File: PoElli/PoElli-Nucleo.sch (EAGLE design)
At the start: 120 parts, among them CN10 NUCLEO-CN10, CN7 NUCLEO-CN7, J3 M022.54MM, J4 M022.54MM, Q3 FDMC2674, Q4 IRFL4310, SW1 A6H2101, SW2 A6H2101, T1 Coilcraft 230NL, T2 FLYBACK750311689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

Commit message: review changes applied
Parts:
- added R10: 100, ELL-i-Passives:R0603
- C21: value 100nF -> 100nF 100V
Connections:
- new net N$9: C21.2, R10.2
- net N$33: now also R10.1; no longer C21.2
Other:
- moved on the sheet: C21, D3, R16
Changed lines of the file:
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@@
 <part name="D3" library="ELL-i-DIscreteSemi" deviceset="BAV20WS" device=""/>
 <part name="R16" library="ELL-i-Passives" deviceset="R" device="1206" value="2k"/>
-<part name="C21" library="ELL-i-Passives" deviceset="C" device="0805" value="100nF"/>
+<part name="C21" library="ELL-i-Passives" deviceset="C" device="0805" value="100nF 100V"/>
 <part name="D17" library="ELL-i-DIscreteSemi" deviceset="DIODE-SCHOTTKY" device="B2100" value="B2100"/>
 <part name="D16" library="ELL-i-DIscreteSemi" deviceset="DIODE-SCHOTTKY" device="B2100" value="B2100"/>
@@
 <part name="D1" library="SparkFun-LED" deviceset="LED-GREEN" device="0603" value="GREEN"/>
 <part name="D2" library="SparkFun-LED" deviceset="LED-YELLOW" device="0603" value="YELLOW"/>
+<part name="R10" library="ELL-i-Passives" deviceset="R" device="0603" value="100"/>
 </parts>
 <sheets>
@@
 <text x="-17.78" y="83.82" size="1.778" layer="97" rot="R180">100V</text>
 <text x="10.16" y="60.96" size="1.778" layer="97">25V</text>
-<text x="2.54" y="104.14" size="1.778" layer="97" rot="R90">100V</text>
 <text x="-68.58" y="96.52" size="1.778" layer="97">R38 solder bridge is a potential
 alternative to R25, D11 and D13.
@@
 <instance part="C30" gate="G$1" x="10.16" y="66.04" rot="R90"/>
 <instance part="R34" gate="G$1" x="-5.08" y="12.7" rot="R90"/>
-<instance part="D3" gate="G$1" x="22.86" y="93.98" rot="R180"/>
-<instance part="R16" gate="G$1" x="-2.54" y="93.98" rot="R180"/>
-<instance part="C21" gate="G$1" x="-5.08" y="101.6" rot="R90"/>
+<instance part="D3" gate="G$1" x="20.32" y="93.98" rot="R180"/>
+<instance part="R16" gate="G$1" x="-5.08" y="93.98" rot="R180"/>
+<instance part="C21" gate="G$1" x="-10.16" y="101.6" rot="R90"/>
 <instance part="D17" gate="G$1" x="-160.02" y="22.86" rot="R90"/>
 <instance part="D16" gate="G$1" x="-165.1" y="22.86" rot="R90"/>
@@
 <instance part="D1" gate="G$1" x="185.42" y="180.34"/>
 <instance part="D2" gate="G$1" x="195.58" y="180.34"/>
+<instance part="R10" gate="G$1" x="2.54" y="101.6" rot="R180"/>
 </instances>
 <busses>
@@
 <junction x="27.94" y="53.34"/>
 <pinref part="D3" gate="G$1" pin="A"/>
-<wire x1="25.4" y1="93.98" x2="27.94" y2="93.98" width="0.1524" layer="91"/>
+<wire x1="22.86" y1="93.98" x2="27.94" y2="93.98" width="0.1524" layer="91"/>
 <junction x="27.94" y="93.98"/>
 <pinref part="T2" gate="G$1" pin="PRI+"/>
@@
 <net name="N$33" class="0">
 <segment>
-<pinref part="C21" gate="G$1" pin="2"/>
-<wire x1="12.7" y1="101.6" x2="0" y2="101.6" width="0.1524" layer="91"/>
 <pinref part="D3" gate="G$1" pin="C"/>
-<wire x1="20.32" y1="93.98" x2="12.7" y2="93.98" width="0.1524" layer="91"/>
-<wire x1="12.7" y1="101.6" x2="12.7" y2="93.98" width="0.1524" layer="91"/>
+<wire x1="17.78" y1="93.98" x2="10.16" y2="93.98" width="0.1524" layer="91"/>
+<wire x1="10.16" y1="101.6" x2="10.16" y2="93.98" width="0.1524" layer="91"/>
 <pinref part="R16" gate="G$1" pin="1"/>
-<wire x1="2.54" y1="93.98" x2="12.7" y2="93.98" width="0.1524" layer="91"/>
-<junction x="12.7" y="93.98"/>
+<wire x1="0" y1="93.98" x2="10.16" y2="93.98" width="0.1524" layer="91"/>
+<junction x="10.16" y="93.98"/>
+<pinref part="R10" gate="G$1" pin="1"/>
+<wire x1="7.62" y1="101.6" x2="10.16" y2="101.6" width="0.1524" layer="91"/>
 </segment>
 </net>
@@
 <wire x1="-40.64" y1="86.36" x2="-15.24" y2="86.36" width="0.1524" layer="91"/>
 <pinref part="U4" gate="G$1" pin="VIN"/>
-<wire x1="-15.24" y1="86.36" x2="-10.16" y2="86.36" width="0.1524" layer="91"/>
 <junction x="-15.24" y="86.36"/>
 <pinref part="C29" gate="G$1" pin="1"/>
 <pinref part="R16" gate="G$1" pin="2"/>
-<wire x1="-10.16" y1="86.36" x2="35.56" y2="86.36" width="0.1524" layer="91"/>
-<wire x1="-7.62" y1="93.98" x2="-10.16" y2="93.98" width="0.1524" layer="91"/>
+<wire x1="-15.24" y1="86.36" x2="35.56" y2="86.36" width="0.1524" layer="91"/>
+<wire x1="-10.16" y1="93.98" x2="-15.24" y2="93.98" width="0.1524" layer="91"/>
 <junction x="-15.24" y="86.36"/>
-<wire x1="-10.16" y1="93.98" x2="-10.16" y2="101.6" width="0.1524" layer="91"/>
-<junction x="-10.16" y="93.98"/>
+<wire x1="-15.24" y1="93.98" x2="-15.24" y2="101.6" width="0.1524" layer="91"/>
+<junction x="-15.24" y="93.98"/>
 <pinref part="C21" gate="G$1" pin="1"/>
-<wire x1="-10.16" y1="101.6" x2="-7.62" y2="101.6" width="0.1524" layer="91"/>
+<wire x1="-15.24" y1="101.6" x2="-12.7" y2="101.6" width="0.1524" layer="91"/>
 <pinref part="T2" gate="G$1" pin="PRI-"/>
 <wire x1="-124.46" y1="2.54" x2="-124.46" y2="86.36" width="0.1524" layer="91"/>
@@
 <pinref part="SUPPLY6" gate="VDD" pin="VDD"/>
 <wire x1="-124.46" y1="91.44" x2="-124.46" y2="86.36" width="0.1524" layer="91"/>
-<wire x1="-10.16" y1="93.98" x2="-10.16" y2="86.36" width="0.1524" layer="91"/>
-<junction x="-10.16" y="86.36"/>
+<wire x1="-15.24" y1="93.98" x2="-15.24" y2="86.36" width="0.1524" layer="91"/>
+<junction x="-15.24" y="86.36"/>
 </segment>
 <segment>
@@
 </segment>
 </net>
+<net name="N$9" class="0">
+<segment>
+<pinref part="C21" gate="G$1" pin="2"/>
+<pinref part="R10" gate="G$1" pin="2"/>
+<wire x1="-5.08" y1="101.6" x2="-2.54" y2="101.6" width="0.1524" layer="91"/>
+</segment>
+</net>

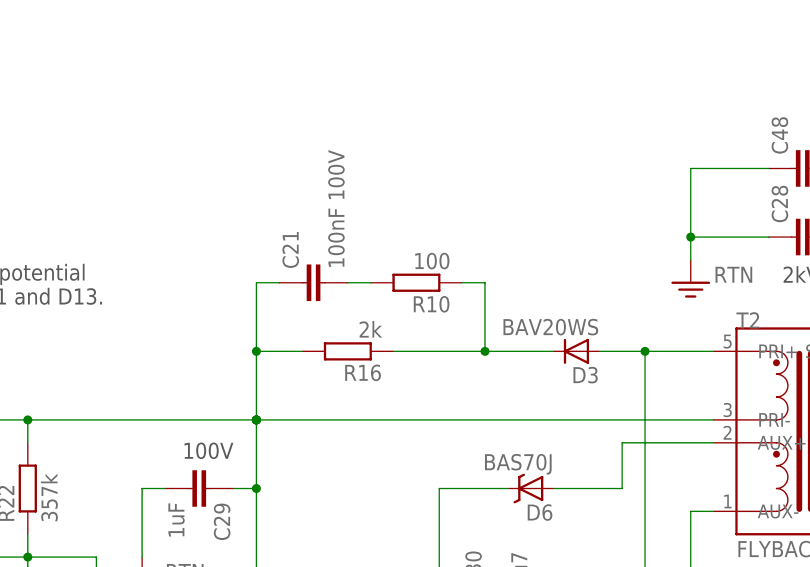
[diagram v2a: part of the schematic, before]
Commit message: Remove R10
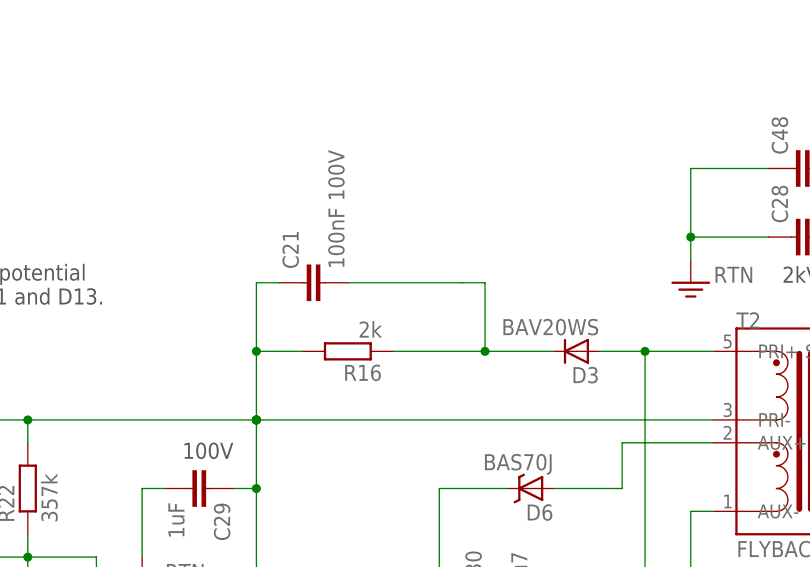
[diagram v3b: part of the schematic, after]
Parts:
- removed R10: 100, ELL-i-Passives:R0603
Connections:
- net N$33: no longer R10.1
- net N$9: no longer R10.2
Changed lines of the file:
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@@
 <part name="D1" library="SparkFun-LED" deviceset="LED-GREEN" device="0603" value="GREEN"/>
 <part name="D2" library="SparkFun-LED" deviceset="LED-YELLOW" device="0603" value="YELLOW"/>
-<part name="R10" library="ELL-i-Passives" deviceset="R" device="0603" value="100"/>
 </parts>
 <sheets>
@@
 <instance part="D1" gate="G$1" x="185.42" y="180.34"/>
 <instance part="D2" gate="G$1" x="195.58" y="180.34"/>
-<instance part="R10" gate="G$1" x="2.54" y="101.6" rot="R180"/>
 </instances>
 <busses>
@@
 <wire x1="0" y1="93.98" x2="10.16" y2="93.98" width="0.1524" layer="91"/>
 <junction x="10.16" y="93.98"/>
-<pinref part="R10" gate="G$1" pin="1"/>
 <wire x1="7.62" y1="101.6" x2="10.16" y2="101.6" width="0.1524" layer="91"/>
 </segment>
@@
 <segment>
 <pinref part="C21" gate="G$1" pin="2"/>
-<pinref part="R10" gate="G$1" pin="2"/>
-<wire x1="-5.08" y1="101.6" x2="-2.54" y2="101.6" width="0.1524" layer="91"/>
-</segment>
-</net>
+<wire x1="7.62" y1="101.6" x2="-5.08" y2="101.6" width="0.1524" layer="91"/>
+</segment>
+</net>

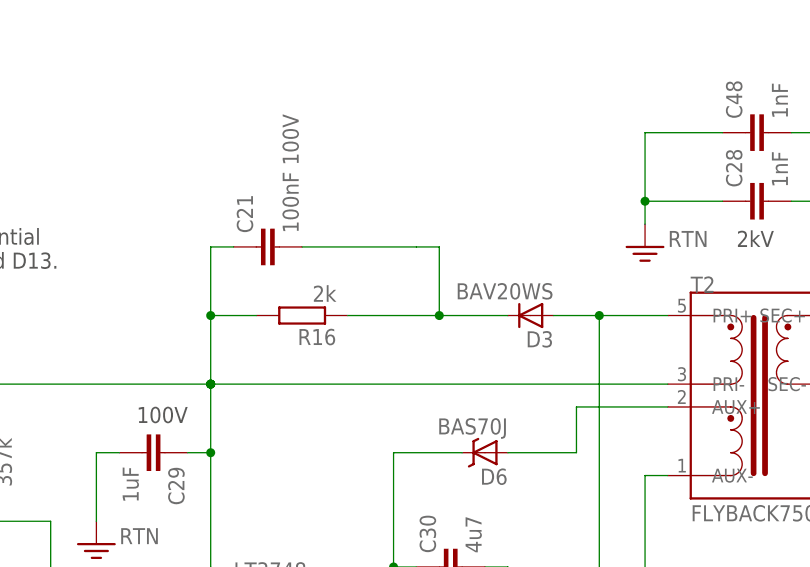
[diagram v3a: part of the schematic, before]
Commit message: Fix broken net between C21 and D3/R16
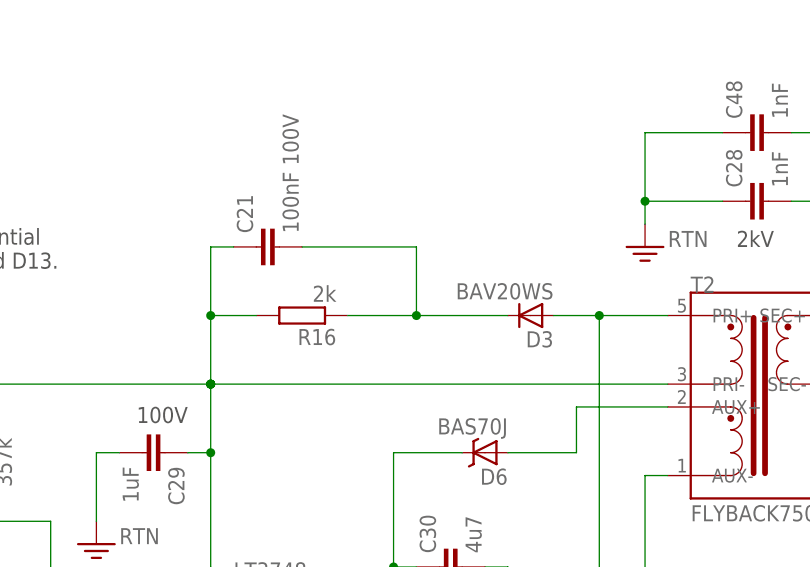
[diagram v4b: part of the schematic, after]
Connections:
- removed net N$9: C21.2
- net N$33: now also C21.2
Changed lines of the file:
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@@
 <segment>
 <pinref part="D3" gate="G$1" pin="C"/>
-<wire x1="17.78" y1="93.98" x2="10.16" y2="93.98" width="0.1524" layer="91"/>
-<wire x1="10.16" y1="101.6" x2="10.16" y2="93.98" width="0.1524" layer="91"/>
 <pinref part="R16" gate="G$1" pin="1"/>
-<wire x1="0" y1="93.98" x2="10.16" y2="93.98" width="0.1524" layer="91"/>
-<junction x="10.16" y="93.98"/>
-<wire x1="7.62" y1="101.6" x2="10.16" y2="101.6" width="0.1524" layer="91"/>
+<wire x1="0" y1="93.98" x2="7.62" y2="93.98" width="0.1524" layer="91"/>
+<pinref part="C21" gate="G$1" pin="2"/>
+<wire x1="7.62" y1="93.98" x2="17.78" y2="93.98" width="0.1524" layer="91"/>
+<wire x1="-5.08" y1="101.6" x2="7.62" y2="101.6" width="0.1524" layer="91"/>
+<wire x1="7.62" y1="101.6" x2="7.62" y2="93.98" width="0.1524" layer="91"/>
+<junction x="7.62" y="93.98"/>
 </segment>
 </net>
@@
 </segment>
 </net>
-<net name="N$9" class="0">
-<segment>
-<pinref part="C21" gate="G$1" pin="2"/>
-<wire x1="7.62" y1="101.6" x2="-5.08" y2="101.6" width="0.1524" layer="91"/>
-</segment>
-</net>

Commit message: Fix mistakes from first prototype round
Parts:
- removed C10: 10nF, ELL-i-Passives:C0402
- added TP12, TP13, TP14, TP15, TP16, TP17, TP18: TEST_POINT-5000, ELL-i-Passives:TEST_POINT-5000
- C12: value 100nF -> 10nF
- C32: value 47uF -> 10uF 100 V; device ELL-i-Passives:CPOL1206 -> ELL-i-Passives:CPOLE
- CN7: value NUCLEO-CN7 -> NUCLEO-CN10; device ELL-i-Boards:NUCLEO-CN7 -> ELL-i-Boards:NUCLEO-CN10
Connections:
- removed net N$44: C12.2, R8.1, R9.1
- new net TPINCT: C12.2, R8.1, R9.1, T1.RCT, TP13.P$1
- net +3V3: now also CN7.PA12_12, CN7.PB12_16; no longer CN7.3V3_12, CN7.3V3_16
- net GNDA: now also CN7.PB2_22; no longer C10.1, CN7.GND_22
- net N$11: now also CN7.1_PC9; no longer CN7.1_PC10
- net N$12: now also CN7.3_PB8; no longer CN7.3_PC12
- net N$13: now also CN7.PC8_2; no longer CN7.PC11_2
- net N$14: now also CN7.PC6_4; no longer CN7.PD2_4
- net N$40: now also TP16.P$1; no longer C10.2, T1.RCT
- net SGND: now also TP18.P$1
- net TPIN+: now also TP14.P$1
- net TPIN-: now also TP12.P$1
- net TPOUT+: now also TP17.P$1
- net TPOUT-: now also TP15.P$1
- net VIN: now also CN7.PB1_24; no longer CN7.VIN_24
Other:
- note added: "C19 close to transformer pins"
- note removed: "C10 and C19 close to transformer pins"

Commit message: rev 3 DRC ok
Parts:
- removed TP12, TP13, TP14, TP15, TP16, TP17: TEST_POINT-5000, ELL-i-Passives:TEST_POINT-5000
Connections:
- net N$40: no longer TP16.P$1
- net TPIN+: no longer TP14.P$1
- net TPIN-: no longer TP12.P$1
- net TPINCT: no longer TP13.P$1
- net TPOUT+: no longer TP17.P$1
- net TPOUT-: no longer TP15.P$1

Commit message: rev 0.3
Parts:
- Q3: value FDMC2674 -> FDMC2674HANDSOLDERING; device ELL-i-DIscreteSemi:FDMC2674 -> ELL-i-DIscreteSemi:FDMC2674HANDSOLDERING
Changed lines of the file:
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@@
 <grid distance="0.1" unitdist="inch" unit="inch" style="lines" multiple="1" display="no" altdistance="0.01" altunitdist="inch" altunit="inch"/>
 <layers>
-<layer number="1" name="Top" color="4" fill="1" visible="no" active="no"/>
-<layer number="16" name="Bottom" color="1" fill="1" visible="no" active="no"/>
-<layer number="17" name="Pads" color="2" fill="1" visible="no" active="no"/>
-<layer number="18" name="Vias" color="2" fill="1" visible="no" active="no"/>
-<layer number="19" name="Unrouted" color="6" fill="1" visible="no" active="no"/>
-<layer number="20" name="Dimension" color="15" fill="1" visible="no" active="no"/>
-<layer number="21" name="tPlace" color="11" fill="1" visible="no" active="no"/>
-<layer number="22" name="bPlace" color="7" fill="1" visible="no" active="no"/>
-<layer number="23" name="tOrigins" color="15" fill="1" visible="no" active="no"/>
-<layer number="24" name="bOrigins" color="15" fill="1" visible="no" active="no"/>
-<layer number="25" name="tNames" color="7" fill="1" visible="no" active="no"/>
-<layer number="26" name="bNames" color="7" fill="1" visible="no" active="no"/>
-<layer number="27" name="tValues" color="7" fill="1" visible="no" active="no"/>
-<layer number="28" name="bValues" color="7" fill="1" visible="no" active="no"/>
+<layer number="1" name="Top" color="4" fill="1" visible="yes" active="no"/>
+<layer number="16" name="Bottom" color="1" fill="1" visible="yes" active="no"/>
+<layer number="17" name="Pads" color="2" fill="1" visible="yes" active="no"/>
+<layer number="18" name="Vias" color="2" fill="1" visible="yes" active="no"/>
+<layer number="19" name="Unrouted" color="6" fill="1" visible="yes" active="no"/>
+<layer number="20" name="Dimension" color="15" fill="1" visible="yes" active="no"/>
+<layer number="21" name="tPlace" color="11" fill="1" visible="yes" active="no"/>
+<layer number="22" name="bPlace" color="7" fill="1" visible="yes" active="no"/>
+<layer number="23" name="tOrigins" color="15" fill="1" visible="yes" active="no"/>
+<layer number="24" name="bOrigins" color="15" fill="1" visible="yes" active="no"/>
+<layer number="25" name="tNames" color="7" fill="1" visible="yes" active="no"/>
+<layer number="26" name="bNames" color="7" fill="1" visible="yes" active="no"/>
+<layer number="27" name="tValues" color="7" fill="1" visible="yes" active="no"/>
+<layer number="28" name="bValues" color="7" fill="1" visible="yes" active="no"/>
 <layer number="29" name="tStop" color="7" fill="3" visible="no" active="no"/>
 <layer number="30" name="bStop" color="7" fill="6" visible="no" active="no"/>
@@
 <layer number="35" name="tGlue" color="7" fill="4" visible="no" active="no"/>
 <layer number="36" name="bGlue" color="7" fill="5" visible="no" active="no"/>
-<layer number="37" name="tTest" color="7" fill="1" visible="no" active="no"/>
-<layer number="38" name="bTest" color="7" fill="1" visible="no" active="no"/>
+<layer number="37" name="tTest" color="7" fill="1" visible="yes" active="no"/>
+<layer number="38" name="bTest" color="7" fill="1" visible="yes" active="no"/>
 <layer number="39" name="tKeepout" color="4" fill="11" visible="no" active="no"/>
 <layer number="40" name="bKeepout" color="1" fill="11" visible="no" active="no"/>
@@
 <layer number="44" name="Drills" color="7" fill="1" visible="no" active="no"/>
 <layer number="45" name="Holes" color="7" fill="1" visible="no" active="no"/>
-<layer number="46" name="Milling" color="3" fill="1" visible="no" active="no"/>
-<layer number="47" name="Measures" color="7" fill="1" visible="no" active="no"/>
-<layer number="48" name="Document" color="7" fill="1" visible="no" active="no"/>
-<layer number="49" name="Reference" color="7" fill="1" visible="no" active="no"/>
-<layer number="50" name="dxf" color="7" fill="1" visible="no" active="no"/>
-<layer number="51" name="tDocu" color="7" fill="1" visible="no" active="no"/>
-<layer number="52" name="bDocu" color="7" fill="1" visible="no" active="no"/>
-<layer number="53" name="tGND_GNDA" color="7" fill="9" visible="no" active="no"/>
-<layer number="54" name="bGND_GNDA" color="1" fill="9" visible="no" active="no"/>
-<layer number="56" name="wert" color="7" fill="1" visible="no" active="no"/>
-<layer number="57" name="tCopper" color="7" fill="1" visible="no" active="no"/>
-<layer number="58" name="bCopper" color="7" fill="1" visible="no" active="no"/>
+<layer number="46" name="Milling" color="3" fill="1" visible="yes" active="no"/>
+<layer number="47" name="Measures" color="7" fill="1" visible="yes" active="no"/>
+<layer number="48" name="Document" color="7" fill="1" visible="yes" active="no"/>
+<layer number="49" name="Reference" color="7" fill="1" visible="yes" active="no"/>
+<layer number="50" name="dxf" color="7" fill="1" visible="yes" active="no"/>
+<layer number="51" name="tDocu" color="7" fill="1" visible="yes" active="no"/>
+<layer number="52" name="bDocu" color="7" fill="1" visible="yes" active="no"/>
+<layer number="53" name="tGND_GNDA" color="7" fill="9" visible="yes" active="no"/>
+<layer number="54" name="bGND_GNDA" color="1" fill="9" visible="yes" active="no"/>
+<layer number="56" name="wert" color="7" fill="1" visible="yes" active="no"/>
+<layer number="57" name="tCopper" color="7" fill="1" visible="yes" active="no"/>
+<layer number="58" name="bCopper" color="7" fill="1" visible="yes" active="no"/>
 <layer number="91" name="Nets" color="2" fill="1" visible="yes" active="yes"/>
 <layer number="92" name="Busses" color="1" fill="1" visible="yes" active="yes"/>
@@
 <part name="C38" library="ELL-i-Passives" deviceset="C" device="0402" value="6n8"/>
 <part name="C39" library="ELL-i-Passives" deviceset="C" device="0402" value="470p"/>
-<part name="Q3" library="ELL-i-DIscreteSemi" deviceset="FDMC2674" device=""/>
+<part name="Q3" library="ELL-i-DIscreteSemi" deviceset="FDMC2674" device="HANDSOLDERING" value="FDMC2674HANDSOLDERING"/>
 <part name="R28" library="ELL-i-Passives" deviceset="R" device="0603" value="0R"/>
 <part name="R30" library="ELL-i-Passives" deviceset="R" device="0603" value="0R"/>
